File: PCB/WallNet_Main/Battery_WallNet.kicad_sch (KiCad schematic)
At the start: 27 parts, among them J101 USB_C_Receptacle_PowerOnly_6P, J102 Conn_01x04_Pin, U101 BQ25895RTWT

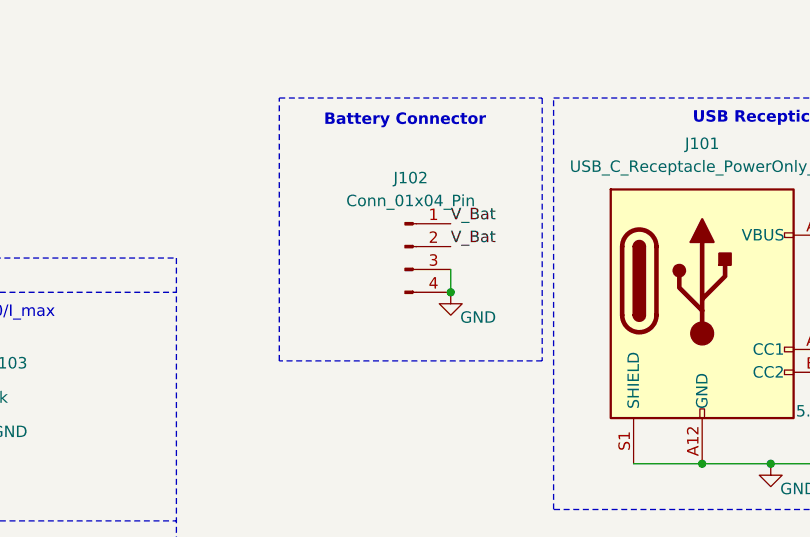
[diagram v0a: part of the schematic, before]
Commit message: updated connectors, added layout guide
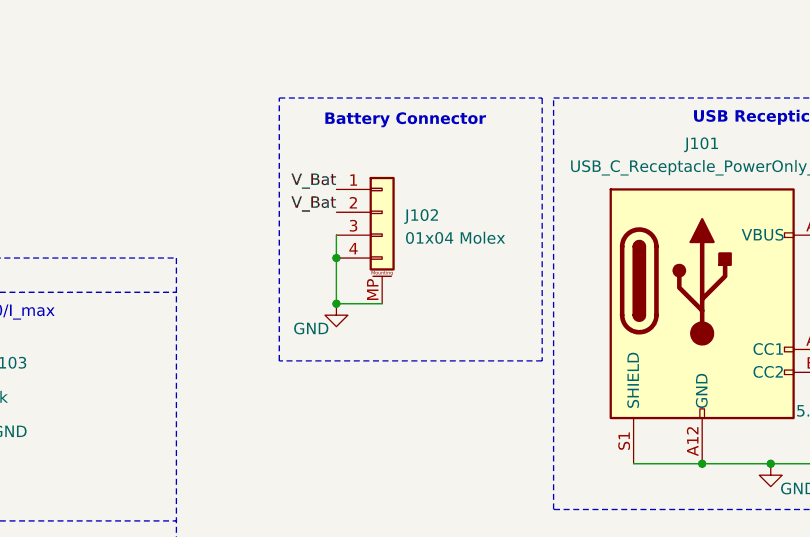
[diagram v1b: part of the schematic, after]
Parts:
- removed J102: Conn_01x04_Pin, Connector_Molex:Molex_PicoBlade_53261-0471_1x04-1MP_P1.25mm_Horizontal, symbol Connector:Conn_01x04_Pin
- added J102: 01x04 Molex, Connector_Molex:Molex_PicoBlade_53261-0471_1x04-1MP_P1.25mm_Horizontal, symbol Connector_Generic_MountingPin:Conn_01x04_MountingPin
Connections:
- net BAT: now also J102.1 (Pin_1), J102.2 (Pin_2)
- net GND: now also J102.3 (Pin_3), J102.4 (Pin_4), J102.MP (MountPin)
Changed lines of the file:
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@@
 	)
 	(junction
-		(at 199.39 44.45)
+		(at 227.33 63.5)
 		(diameter 0)
 		(color 0 0 0 0)
 	)
 	(junction
-		(at 227.33 63.5)
+		(at 123.19 119.38)
 		(diameter 0)
 		(color 0 0 0 0)
 	)
 	(junction
-		(at 123.19 119.38)
+		(at 186.69 40.64)
 		(diameter 0)
 		(color 0 0 0 0)
@@
 		(color 0 0 0 0)
 	)
+	(junction
+		(at 186.69 45.72)
+		(diameter 0)
+		(color 0 0 0 0)
+	)
 	(no_connect
 		(at 71.12 88.9)
@@
 	(wire
 		(pts
+			(xy 186.69 38.1) (xy 186.69 40.64)
+		)
+		(stroke
+			(width 0)
+			(type default)
+		)
+	)
+	(wire
+		(pts
 			(xy 248.92 63.5) (xy 248.92 58.42)
 		)
@@
 	(wire
 		(pts
+			(xy 186.69 45.72) (xy 191.77 45.72)
+		)
+		(stroke
+			(width 0)
+			(type default)
+		)
+	)
+	(wire
+		(pts
 			(xy 135.89 74.93) (xy 137.16 74.93)
 		)
@@
 	(wire
 		(pts
+			(xy 186.69 45.72) (xy 186.69 40.64)
+		)
+		(stroke
+			(width 0)
+			(type default)
+		)
+	)
+	(wire
+		(pts
 			(xy 71.12 58.42) (xy 71.12 60.96)
 		)
@@
 	(wire
 		(pts
-			(xy 199.39 41.91) (xy 199.39 44.45)
-		)
-		(stroke
-			(width 0)
-			(type default)
-		)
-	)
-	(wire
-		(pts
 			(xy 142.24 96.52) (xy 143.51 96.52)
 		)
@@
 		)
 	)
+	(label "V_Bat"
+		(at 186.69 35.56 180)
+		(effects
+			(font
+				(size 1.27 1.27)
+			)
+			(justify right bottom)
+		)
+	)
 	(label "BTST"
 		(at 71.12 81.28 0)
@@
 		)
 	)
-	(label "V_Bat"
-		(at 199.39 39.37 0)
-		(effects
-			(font
-				(size 1.27 1.27)
-			)
-			(justify left bottom)
-		)
-	)
-	(label "V_Bat"
-		(at 199.39 36.83 0)
-		(effects
-			(font
-				(size 1.27 1.27)
-			)
-			(justify left bottom)
-		)
-	)
 	(label "BQ_SDA"
 		(at 43.18 26.67 0)
@@
 		)
 	)
+	(label "V_Bat"
+		(at 186.69 33.02 180)
+		(effects
+			(font
+				(size 1.27 1.27)
+			)
+			(justify right bottom)
+		)
+	)
 	(label "CE"
 		(at 113.03 95.25 180)
@@
 	(symbol
 		(lib_id "power:GND")
-		(at 199.39 44.45 0)
+		(at 186.69 45.72 0)
 		(unit 1)
 		(exclude_from_sim no)
@@
 		(dnp no)
 		(property "Reference" "#PWR012"
-			(at 199.39 50.8 0)
+			(at 186.69 52.07 0)
 			(effects
 				(font
@@
 		)
 		(property "Value" "GND"
-			(at 202.438 47.244 0)
+			(at 183.896 48.514 0)
 			(effects
 				(font
@@
 		)
 		(property "Footprint" ""
-			(at 199.39 44.45 0)
+			(at 186.69 45.72 0)
 			(effects
 				(font
@@
 		)
 		(property "Datasheet" ""
-			(at 199.39 44.45 0)
+			(at 186.69 45.72 0)
 			(effects
 				(font
@@
 		)
 		(property "Description" "Power symbol creates a global label with name \"GND\" , ground"
-			(at 199.39 44.45 0)
+			(at 186.69 45.72 0)
 			(effects
 				(font
@@
 	)
 	(symbol
+		(lib_id "Connector_Generic_MountingPin:Conn_01x04_MountingPin")
+		(at 191.77 35.56 0)
+		(unit 1)
+		(exclude_from_sim no)
+		(in_bom yes)
+		(on_board yes)
+		(dnp no)
+		(fields_autoplaced yes)
+		(property "Reference" "J102"
+			(at 194.31 35.9155 0)
+			(effects
+				(font
+					(size 1.27 1.27)
+				)
+				(justify left)
+			)
+		)
+		(property "Value" "01x04 Molex"
+			(at 194.31 38.4555 0)
+			(effects
+				(font
+					(size 1.27 1.27)
+				)
+				(justify left)
+			)
+		)
+		(property "Footprint" "Connector_Molex:Molex_PicoBlade_53261-0471_1x04-1MP_P1.25mm_Horizontal"
+			(at 191.77 35.56 0)
+			(effects
+				(font
+					(size 1.27 1.27)
+				)
+				(hide yes)
+			)
+		)
+		(property "Datasheet" "~"
+			(at 191.77 35.56 0)
+			(effects
+				(font
+					(size 1.27 1.27)
+				)
+				(hide yes)
+			)
+		)
+		(property "Description" "Generic connectable mounting pin connector, single row, 01x04, script generated (kicad-library-utils/schlib/autogen/connector/)"
+			(at 191.77 35.56 0)
+			(effects
+				(font
+					(size 1.27 1.27)
+				)
+				(hide yes)
+			)
+		)
+		(pin "3"
+		)
+		(pin "1"
+		)
+		(pin "2"
+		)
+		(pin "MP"
+		)
+		(pin "4"
+		)
+		(instances
+			(project ""
+				(path "/3272dd14-9e34-4275-b10b-c06dab1b3ca1/ac25aec4-60b5-4d7f-9f99-a074eef21076"
+					(reference "J102")
+					(unit 1)
+				)
+			)
+		)
+	)
+	(symbol
 		(lib_id "power:GND")
 		(at 106.68 95.25 0)
@@
 					(unit 1)
 				)
-			)
-		)
-	)
-	(symbol
-		(lib_id "Connector:Conn_01x04_Pin")
-		(at 194.31 39.37 0)
-		(unit 1)
-		(exclude_from_sim no)
-		(in_bom yes)
-		(on_board yes)
-		(dnp no)
-		(fields_autoplaced yes)
-		(property "Reference" "J102"
-			(at 194.945 31.75 0)
-			(effects
-				(font
-					(size 1.27 1.27)
-				)
-			)
-		)
-		(property "Value" "Conn_01x04_Pin"
-			(at 194.945 34.29 0)
-			(effects
-				(font
-					(size 1.27 1.27)
-				)
-			)
-		)
-		(property "Footprint" "Connector_Molex:Molex_PicoBlade_53261-0471_1x04-1MP_P1.25mm_Horizontal"
-			(at 194.31 39.37 0)
-			(effects
-				(font
-					(size 1.27 1.27)
-				)
-				(hide yes)
-			)
-		)
-		(property "Datasheet" "~"
-			(at 194.31 39.37 0)
-			(effects
-				(font
-					(size 1.27 1.27)
-				)
-				(hide yes)
-			)
-		)
-		(property "Description" "Generic connector, single row, 01x04, script generated"
-			(at 194.31 39.37 0)
-			(effects
-				(font
-					(size 1.27 1.27)
-				)
-				(hide yes)
-			)
-		)
-		(pin "1"
-		)
-		(pin "2"
-		)
-		(pin "4"
-		)
-		(pin "3"
-		)
-		(instances
-			(project "WallNet_Main"
-				(path "/3272dd14-9e34-4275-b10b-c06dab1b3ca1/ac25aec4-60b5-4d7f-9f99-a074eef21076"
-					(reference "J102")
-					(unit 1)
-				)

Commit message: Redid PCB still need to DRC the design
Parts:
- removed TP104: BQ_SDA, 5001:KEYSTONE_5001, symbol Connector:TestPoint
- removed TP105: BQ_SCL, 5001:KEYSTONE_5001, symbol Connector:TestPoint
- removed TP106: BQ_INT, 5001:KEYSTONE_5001, symbol Connector:TestPoint
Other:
- note removed: "Test Points"

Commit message: Fixed minor Issues
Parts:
- C105: value 4.7uF -> 47nF
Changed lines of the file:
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@@
 			)
 		)
-		(property "Value" "4.7uF"
+		(property "Value" "47nF"
 			(at 107.95 123.1962 0)
 			(effects
